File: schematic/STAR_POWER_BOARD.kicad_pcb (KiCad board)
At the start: 4 copper layers, 96.2 x 92.9 mm, 65 parts, among them J1 1017491, J2 1017491, J3 USB4216-03-A, J4 1017491, J5 1017491, Q1 CSD18540Q5B, Q2 CSD17577Q3A, Q3 CSD17577Q3A, Q4 CSD18540Q5B, Q5 SSM6J507NU-LF, U1 TPS566238PRQFR, U2 TPS566238PRQFR, U3 TPS40305DRCT

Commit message: initial commit of branch
added in schematic updates
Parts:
- moved C30 15.4 mm to (139.0, 65.8), turned to 90 degrees
- moved C32 15.2 mm to (148.0, 66.6), turned to 90 degrees
- moved C27 14.0 mm to (145.3, 65.8), turned to 90 degrees
- moved C25 13.3 mm to (142.1, 65.8), turned to 90 degrees
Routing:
- net GND: vias 128 -> 133
- net /PACK+: vias 127 -> 49

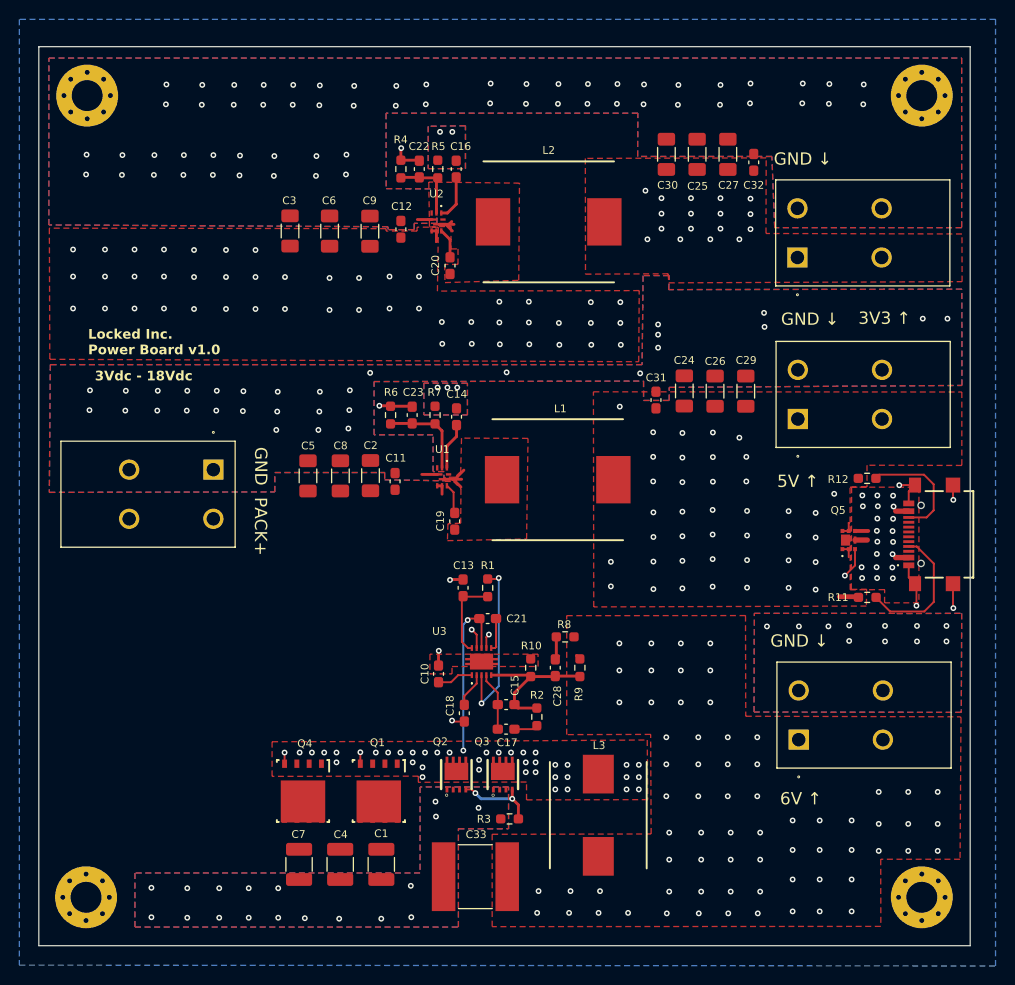
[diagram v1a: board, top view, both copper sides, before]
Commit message: Still incomplete
needs less bottle necks, better via grids, and fix fuse net albels
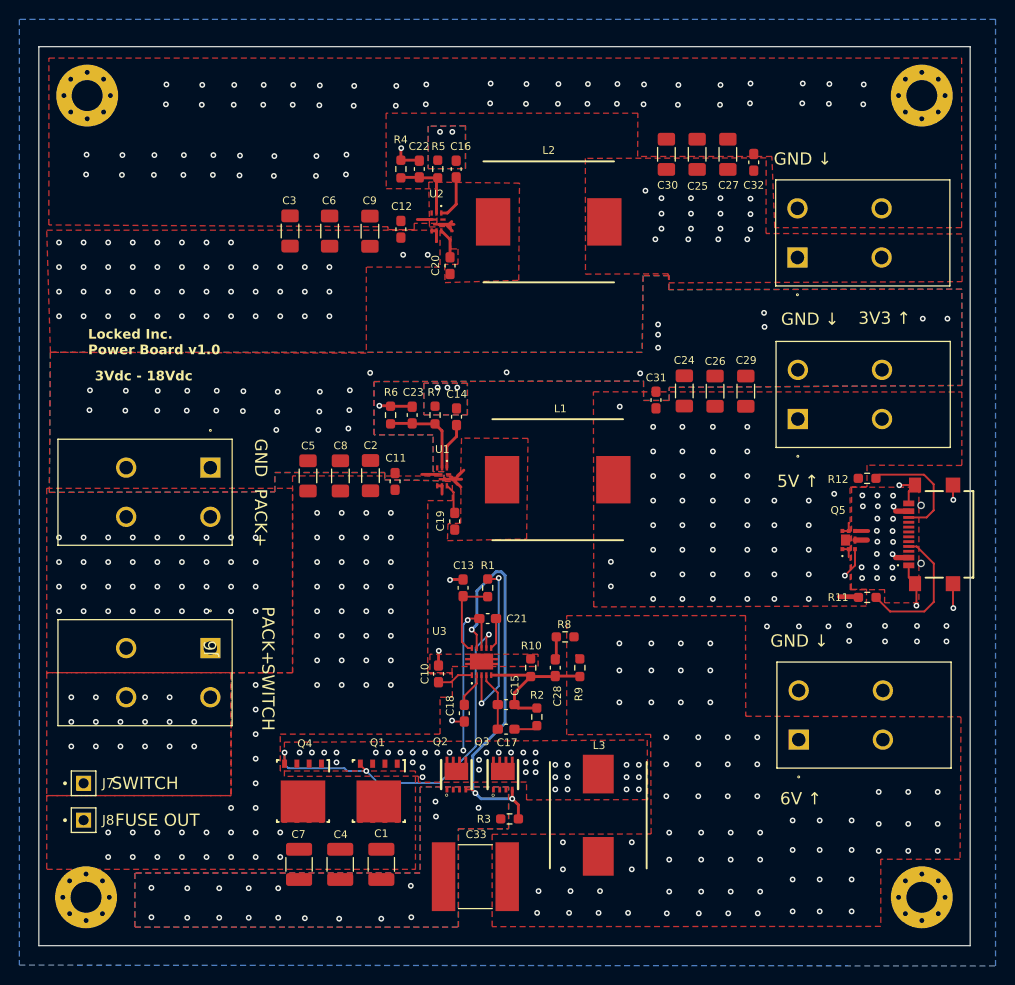
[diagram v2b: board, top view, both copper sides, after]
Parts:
- added J6: 1017491, 1017491:1017491, F.Cu at (91.8, 116.8)
- added J7: Conn_01x01, 861400011YO2LF:AMPHENOL_861400011YO2LF, F.Cu at (78.7, 130.8)
- added J8: Conn_01x01, 861400011YO2LF:AMPHENOL_861400011YO2LF, F.Cu at (78.7, 134.6)
- moved J2 0.37 mm to (91.8, 98.2)
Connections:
- C1 pad 1: /PACK+ -> /FUSE+
- C10 pad 1: /PACK+ -> /FUSE+
- C11 pad 1: /PACK+ -> /FUSE+
- C12 pad 1: /PACK+ -> /FUSE+
- C2 pad 1: /PACK+ -> /FUSE+
- C3 pad 1: /PACK+ -> /FUSE+
- C4 pad 1: /PACK+ -> /FUSE+
- C5 pad 1: /PACK+ -> /FUSE+
- C6 pad 1: /PACK+ -> /FUSE+
- C7 pad 1: /PACK+ -> /FUSE+
- C8 pad 1: /PACK+ -> /FUSE+
- C9 pad 1: /PACK+ -> /FUSE+
- Q1 pad 5: /PACK+ -> /FUSE+
- Q1 pad 6: /PACK+ -> /FUSE+
- Q1 pad 7: /PACK+ -> /FUSE+
- Q1 pad 8: /PACK+ -> /FUSE+
- Q1 pad 9: /PACK+ -> /FUSE+
- Q4 pad 5: /PACK+ -> /FUSE+
- Q4 pad 6: /PACK+ -> /FUSE+
- Q4 pad 7: /PACK+ -> /FUSE+
- Q4 pad 8: /PACK+ -> /FUSE+
- Q4 pad 9: /PACK+ -> /FUSE+
- U1 pad 5: /PACK+ -> /FUSE+
- U1 pad 6: /PACK+ -> /FUSE+
- U2 pad 5: /PACK+ -> /FUSE+
- U2 pad 6: /PACK+ -> /FUSE+
- U3 pad 1: /PACK+ -> /FUSE+
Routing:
- net /6V0_LDRV: track 32.3 -> 43.6 mm
- net /PACK+: track 7.12 -> 0.00 mm, vias 49 -> 36
- net /FUSE+: track 0.00 -> 7.12 mm, vias 0 -> 101
- net /6V0_HDRV: track 36.8 -> 39.1 mm
- net /SWITCH_OUT: vias 0 -> 16
- net /P6V0_BUCK: vias 68 -> 72
- net /P5V0_BUCK: vias 41 -> 47
- added copper zone on In2.Cu, net /3V3_SW
- added copper zone on In2.Cu, net /5V0_SW
- added copper zone on F.Cu, net /FUSE+
- added copper zone on In2.Cu, net /FUSE+
- added copper zone on F.Cu, net /SWITCH_OUT
- added copper zone on In2.Cu, net /SWITCH_OUT
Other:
- board text added: "FUSE OUT"
- board text added: "SWITCH"

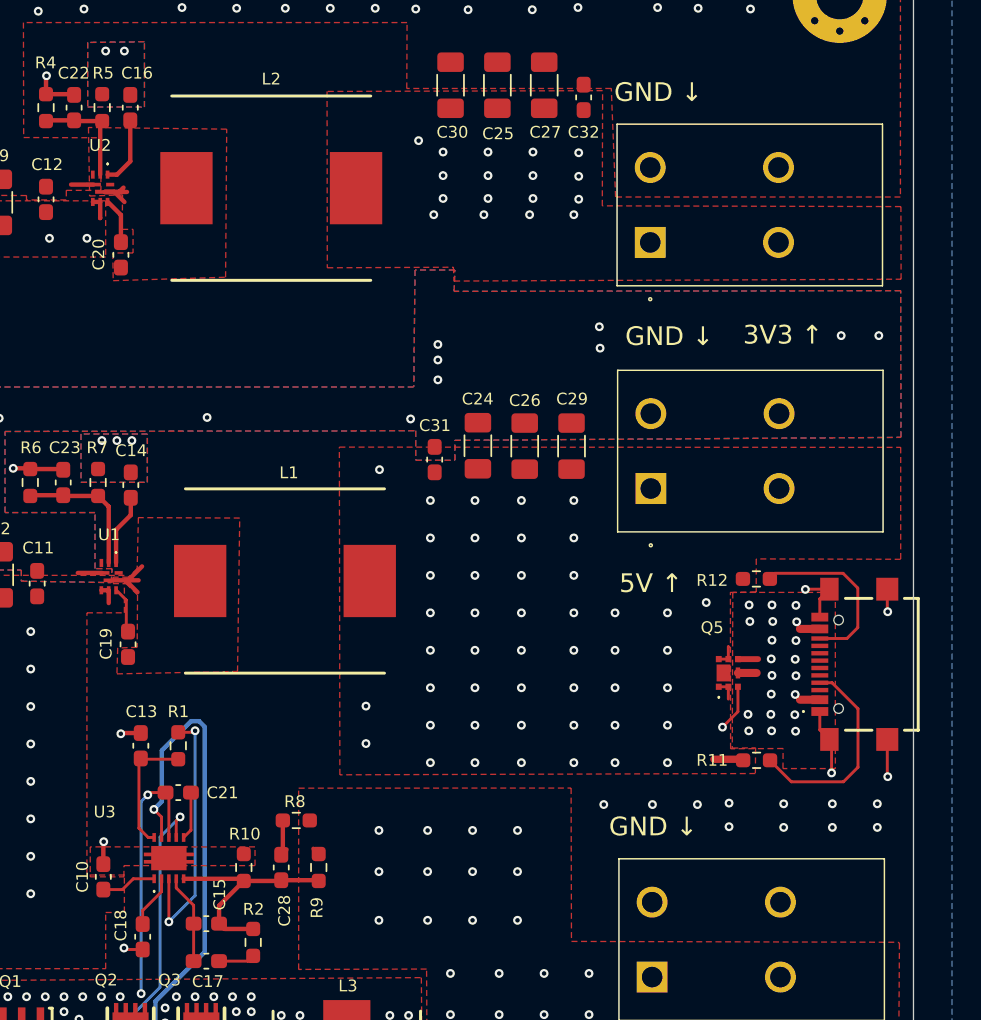
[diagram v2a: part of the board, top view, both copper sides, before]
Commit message: only change left is fixing fuse pads
need to fix fuse pads only
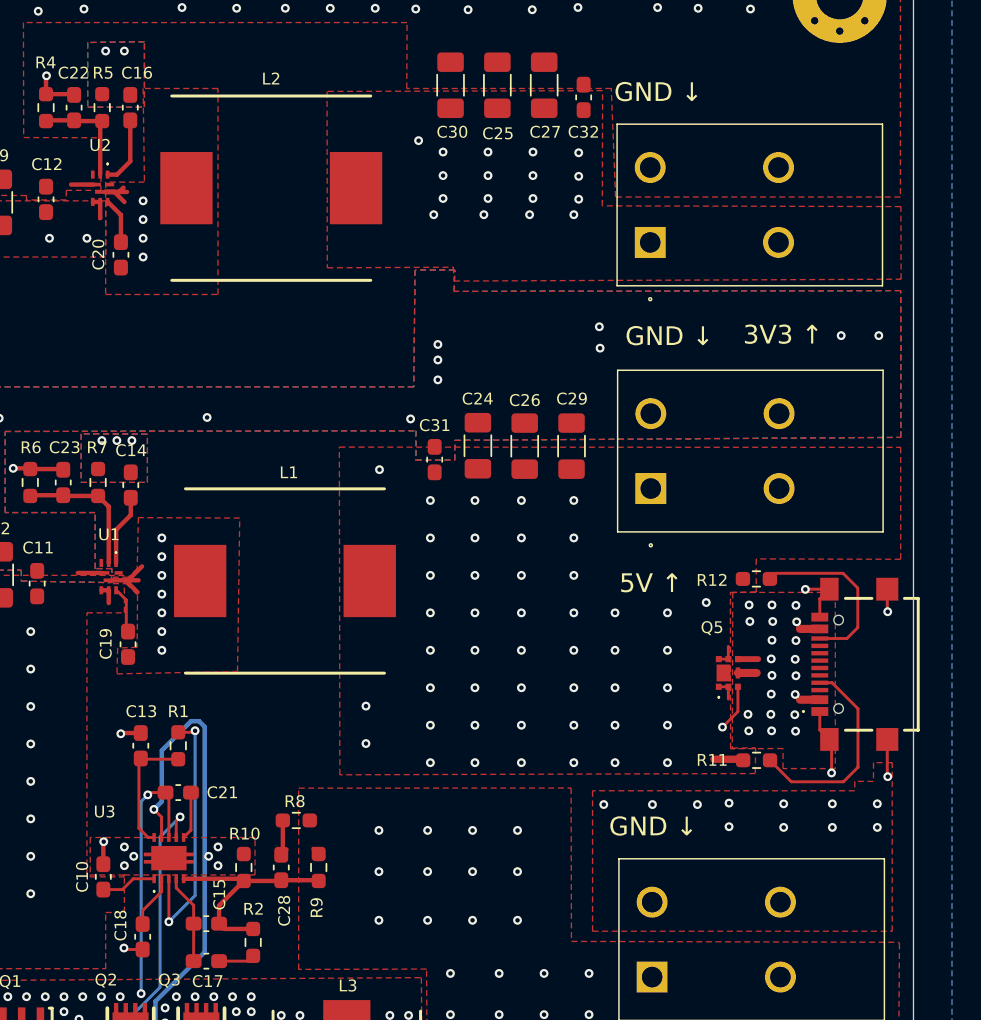
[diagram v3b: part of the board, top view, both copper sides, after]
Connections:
- J7 pad 01: /SWITCH_OUT -> (no net)
- J8 pad 01: /FUSE+ -> (no net)
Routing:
- net /P5V0_BUCK: track 34.2 -> 33.5 mm
- net GND: vias 133 -> 139
- net /5V0_SW: vias 0 -> 7
- net /3V3_SW: vias 0 -> 4
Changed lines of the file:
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@@
 			(layers "*.Cu" "*.Mask")
 			(remove_unused_layers no)
-			(net 39 "/SWITCH_OUT")
 			(solder_mask_margin 0.102)
 		)
@@
 			(layers "*.Cu" "*.Mask")
 			(remove_unused_layers no)
-			(net 38 "/FUSE+")
 			(solder_mask_margin 0.102)
 		)
@@
 	)
 	(via
+		(at 123.19 118.745)
+		(size 0.6)
+		(drill 0.3)
+		(layers "F.Cu" "B.Cu")
+		(net 4)
+	)
+	(via
 		(at 98.45 66)
 		(size 0.6)
@@
 	)
 	(via
+		(at 122.555 118.11)
+		(size 0.6)
+		(drill 0.3)
+		(layers "F.Cu" "B.Cu")
+		(free yes)
+		(net 4)
+	)
+	(via
 		(at 157.4 109.35)
 		(size 0.6)
@@
 	)
 	(via
+		(at 116.84 117.475)
+		(size 0.6)
+		(drill 0.3)
+		(layers "F.Cu" "B.Cu")
+		(net 4)
+	)
+	(via
 		(at 164.852 114.55)
 		(size 0.6)
@@
 	)
 	(via
+		(at 123.19 117.475)
+		(size 0.6)
+		(drill 0.3)
+		(layers "F.Cu" "B.Cu")
+		(net 4)
+	)
+	(via
 		(at 95.2 92.35)
 		(size 0.6)
@@
 	)
 	(via
+		(at 116.84 118.745)
+		(size 0.6)
+		(drill 0.3)
+		(layers "F.Cu" "B.Cu")
+		(net 4)
+	)
+	(via
 		(at 95.25 90.3)
 		(size 0.6)
@@
 	)
 	(via
+		(at 117.475 118.11)
+		(size 0.6)
+		(drill 0.3)
+		(layers "F.Cu" "B.Cu")
+		(net 4)
+	)
+	(via
 		(at 89.402 92.3)
 		(size 0.6)
@@
 		(net 9)
 	)
+	(via
+		(at 118.11 74.93)
+		(size 0.6)
+		(drill 0.3)
+		(layers "F.Cu" "B.Cu")
+		(free yes)
+		(net 9)
+	)
+	(via
+		(at 118.11 76.2)
+		(size 0.6)
+		(drill 0.3)
+		(layers "F.Cu" "B.Cu")
+		(free yes)
+		(net 9)
+	)
+	(via
+		(at 118.11 77.47)
+		(size 0.6)
+		(drill 0.3)
+		(layers "F.Cu" "B.Cu")
+		(free yes)
+		(net 9)
+	)
+	(via
+		(at 118.11 73.66)
+		(size 0.6)
+		(drill 0.3)
+		(layers "F.Cu" "B.Cu")
+		(free yes)
+		(net 9)
+	)
 	(segment
 		(start 111.525 65.215)
@@
 	)
 	(segment
-		(start 110.55 90.55)
-		(end 132.8 90.55)
+		(start 133.69 91.44)
+		(end 134.14 91.89)
 		(width 0.3)
 		(layer "In2.Cu")
@@
 	)
 	(segment
-		(start 109.3 91.8)
-		(end 110.55 90.55)
+		(start 109.66 91.44)
+		(end 133.69 91.44)
 		(width 0.3)
 		(layer "In2.Cu")
@@
 	)
 	(segment
-		(start 132.8 90.55)
-		(end 134.14 91.89)
+		(start 109.3 91.8)
+		(end 109.66 91.44)
 		(width 0.3)
 		(layer "In2.Cu")
@@
 		(net 17)
 	)
+	(via
+		(at 119.38 101.6)
+		(size 0.6)
+		(drill 0.3)
+		(layers "F.Cu" "B.Cu")
+		(free yes)
+		(net 17)
+	)
+	(via
+		(at 119.38 99.06)
+		(size 0.6)
+		(drill 0.3)
+		(layers "F.Cu" "B.Cu")
+		(free yes)
+		(net 17)
+	)
+	(via
+		(at 119.38 96.52)
+		(size 0.6)
+		(drill 0.3)
+		(layers "F.Cu" "B.Cu")
+		(free yes)
+		(net 17)
+	)
+	(via
+		(at 119.38 97.79)
+		(size 0.6)
+		(drill 0.3)
+		(layers "F.Cu" "B.Cu")
+		(free yes)
+		(net 17)
+	)
+	(via
+		(at 119.38 104.14)
+		(size 0.6)
+		(drill 0.3)
+		(layers "F.Cu" "B.Cu")
+		(free yes)
+		(net 17)
+	)
+	(via
+		(at 119.38 100.33)
+		(size 0.6)
+		(drill 0.3)
+		(layers "F.Cu" "B.Cu")
+		(free yes)
+		(net 17)
+	)
+	(via
+		(at 119.38 102.87)
+		(size 0.6)
+		(drill 0.3)
+		(layers "F.Cu" "B.Cu")
+		(free yes)
+		(net 17)
+	)
 	(segment
 		(start 115.335 68.2515)
@@
 	)
 	(zone
+		(net 4)
+		(net_name "GND")
+		(layer "F.Cu")
+		(hatch edge 0.5)
+		(priority 18)
+		(connect_pads yes
+			(clearance 0.5)
+		)
+		(min_thickness 0.25)
+		(filled_areas_thickness no)
+		(fill yes
+			(thermal_gap 0.5)
+			(thermal_bridge_width 0.5)
+		)
+		(polygon
+			(pts
+				(xy 148.59 113.665) (xy 148.59 123.19) (xy 168.91 123.19) (xy 168.91 111.76) (xy 167.64 111.76)
+				(xy 167.64 113.03) (xy 166.37 113.03) (xy 166.37 113.665)
+			)
+		)
+	)
+	(zone
 		(net 38)
 		(net_name "/FUSE+")
@@
 		(polygon
 			(pts
-				(xy 114.524 117.47144) (xy 114.524 119.50344) (xy 116.81 119.50344) (xy 116.81 118.74144) (xy 125.7 118.74144)
-				(xy 125.7 117.47144)
+				(xy 114.524 116.83644) (xy 114.524 119.50344) (xy 116.81 119.50344) (xy 116.81 119.37644) (xy 125.7 119.37644)
+				(xy 125.7 116.83644)
 			)
 		)
@@
 	)
 	(zone
-		(net 9)
-		(net_name "/3V3_SW")
+		(net 28)
+		(net_name "/PACK+")
 		(layers "F.Cu" "In2.Cu")
 		(hatch edge 0.5)
-		(priority 1)
+		(priority 4)
 		(connect_pads yes
 			(clearance 0.5)
@@
 			(thermal_gap 0.5)
 			(thermal_bridge_width 0.5)
+			(island_removal_mode 1)
+			(island_area_min 9.999999)
 		)
 		(polygon
 			(pts
-				(xy 123.778637 68.798479) (xy 114.4048 68.6852) (xy 114.481 73.3334) (xy 116.7162 73.2572) (xy 116.6908 75.594)
-				(xy 117.4274 75.594) (xy 117.4274 77.1942) (xy 116.0558 77.1942) (xy 116.0812 79.0738) (xy 123.702748 78.841081)
+				(xy 74.93 100.33) (xy 74.93 119.38) (xy 100.33 119.38) (xy 100.33 100.33)
 			)
 		)
 	)
 	(zone
-		(net 28)
-		(net_name "/PACK+")
+		(net 37)
+		(net_name "/USBC_VBUS")
 		(layers "F.Cu" "In2.Cu")
 		(hatch edge 0.5)
-		(priority 4)
-		(connect_pads yes
+		(connect_pads
 			(clearance 0.5)
 		)
@@
 			(thermal_gap 0.5)
 			(thermal_bridge_width 0.5)
-			(island_removal_mode 1)
-			(island_area_min 9.999999)
 		)
 		(polygon
 			(pts
-				(xy 74.93 100.33) (xy 74.93 119.38) (xy 100.33 119.38) (xy 100.33 100.33)
+				(xy 157.936334 100.2132) (xy 165.052 100.2132) (xy 165.052 102.302) (xy 165.052 112.16) (xy 161.502879 112.16)
+				(xy 161.51 110.8) (xy 157.95 110.817519)
 			)
 		)
 	)
 	(zone
-		(net 37)
-		(net_name "/USBC_VBUS")
+		(net 9)
+		(net_name "/3V3_SW")
 		(layers "F.Cu" "In2.Cu")
 		(hatch edge 0.5)
-		(connect_pads
+		(priority 1)
+		(connect_pads yes
 			(clearance 0.5)
 		)
@@
 			(thermal_gap 0.5)
 			(thermal_bridge_width 0.5)
+			(island_removal_mode 1)
+			(island_area_min 9.999999)
 		)
 		(polygon
 			(pts
-				(xy 157.936334 100.2132) (xy 165.052 100.2132) (xy 165.052 102.302) (xy 165.052 112.16) (xy 161.502879 112.16)
-				(xy 161.51 110.8) (xy 157.95 110.817519)
+				(xy 115.57 80.01) (xy 123.19 80.01) (xy 123.19 66.04) (xy 118.11 66.04) (xy 118.2 72.39) (xy 115.57 72.39)
 			)
 		)

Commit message: done
done
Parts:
- removed J8: Conn_01x01, 861400011YO2LF:AMPHENOL_861400011YO2LF
- J7: value Conn_01x01 -> 1017491; footprint 861400011YO2LF:AMPHENOL_861400011YO2LF -> 1017491:1017491
- moved J7 12.6 mm to (91.2, 129.5), turned to -90 degrees
- moved J6 2.22 mm to (91.2, 114.7)
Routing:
- net GND: vias 139 -> 152
- net /PACK+: vias 36 -> 27
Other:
- board text added: "FUSE"
- board text removed: "FUSE OUT"

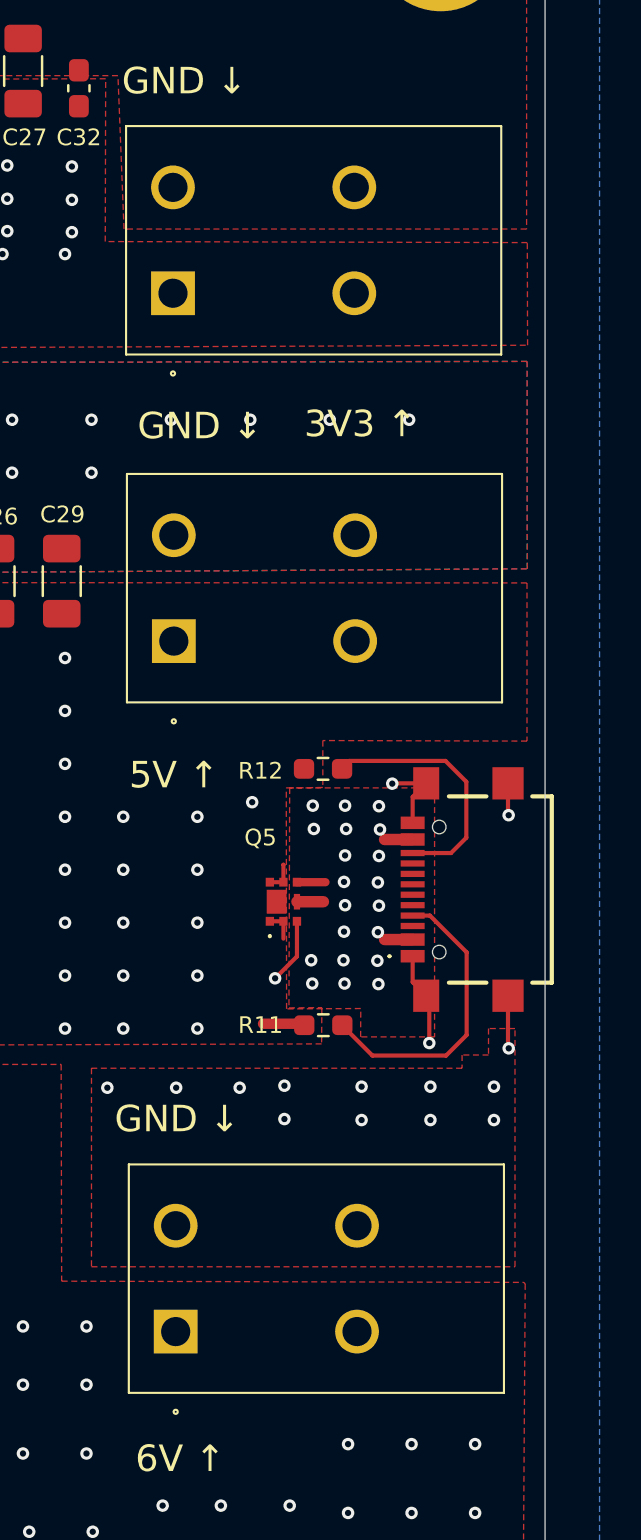
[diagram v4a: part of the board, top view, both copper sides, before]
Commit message: Changed the screw in terminals
Changed screw in terminals
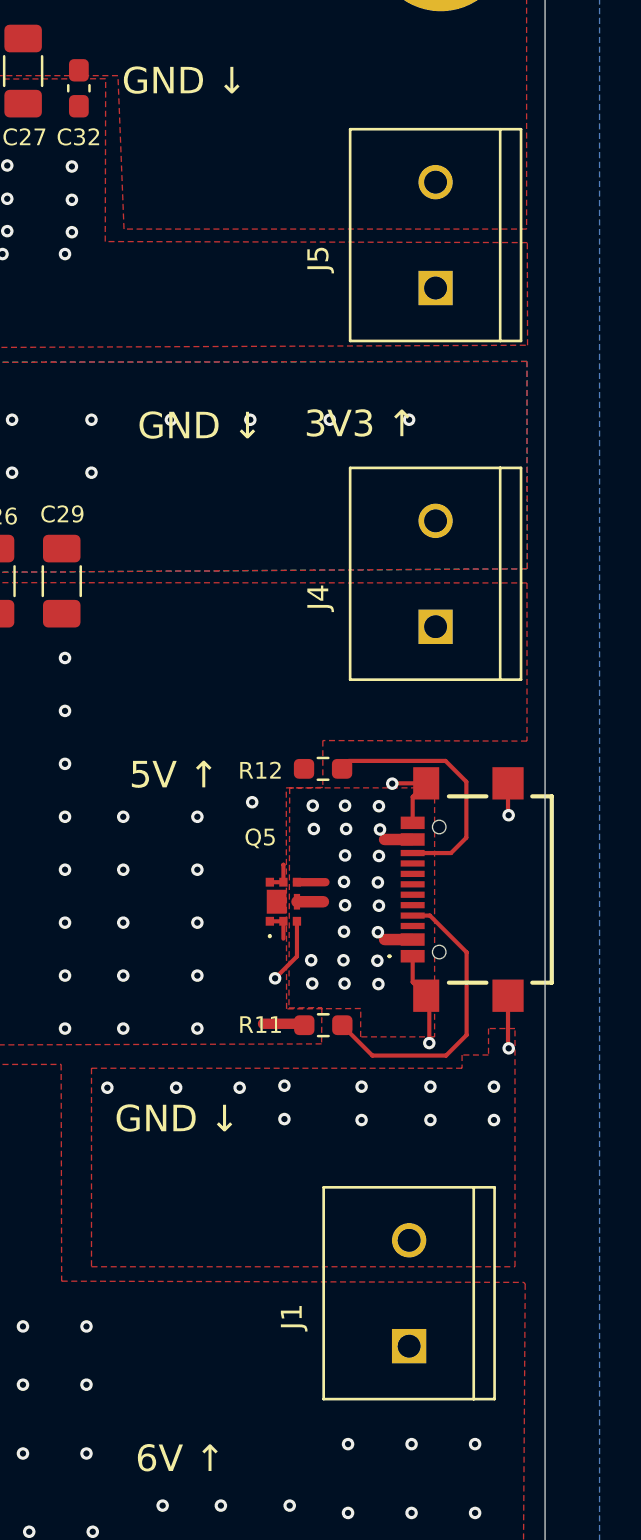
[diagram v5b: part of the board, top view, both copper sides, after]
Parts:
- J1, J4, J5: value 1017491 -> Screw_Terminal_01x02; footprint 1017491:1017491 -> 282837_2:TE_282837-2
- moved J4 13.0 mm to (165.1, 89.9)
- moved J5 12.9 mm to (165.1, 73.7)
- moved J1 11.4 mm to (163.8, 124.5)
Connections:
- J1 pad 2: /P6V0_BUCK -> GND
- J4 pad 2: /P5V0_BUCK -> GND
- J5 pad 2: /P3V3_BUCK -> GND
